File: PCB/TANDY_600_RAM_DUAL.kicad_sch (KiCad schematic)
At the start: 7 parts, among them CN1 TANDY_600_RAM_BUS, CN2 TANDY_600_RAM_BUS, U1 AS6C4008, U2 74HC148, U3 74LVC1G02

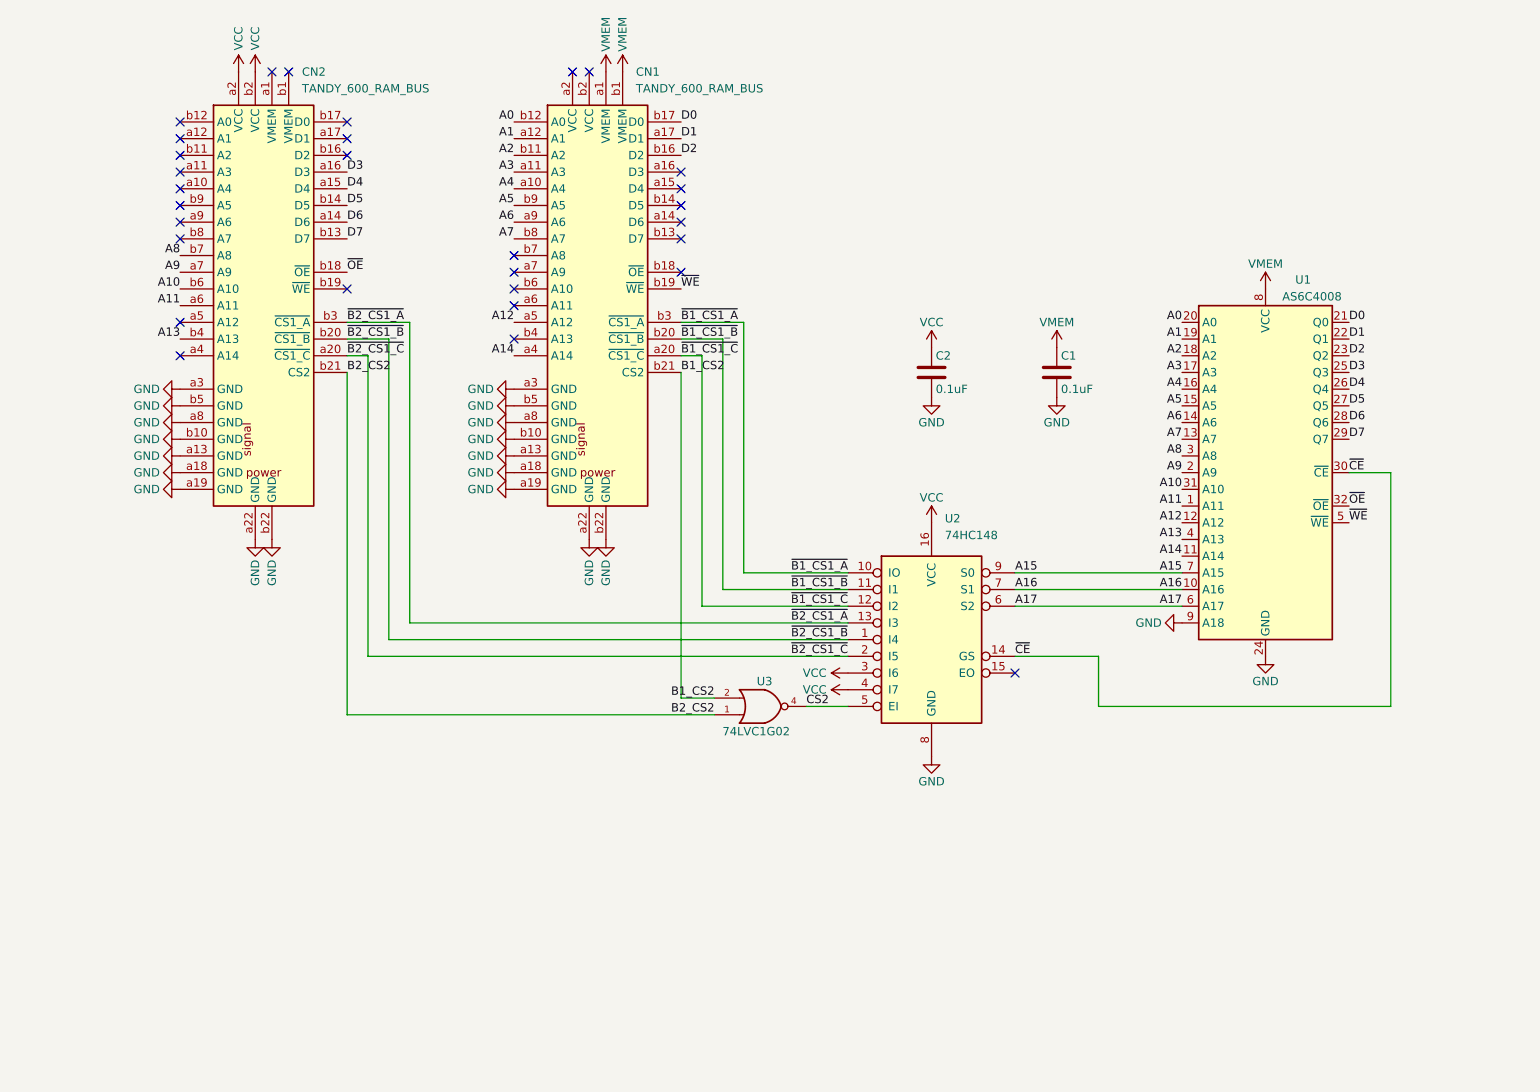
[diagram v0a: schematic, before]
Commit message: footprints, ground paths
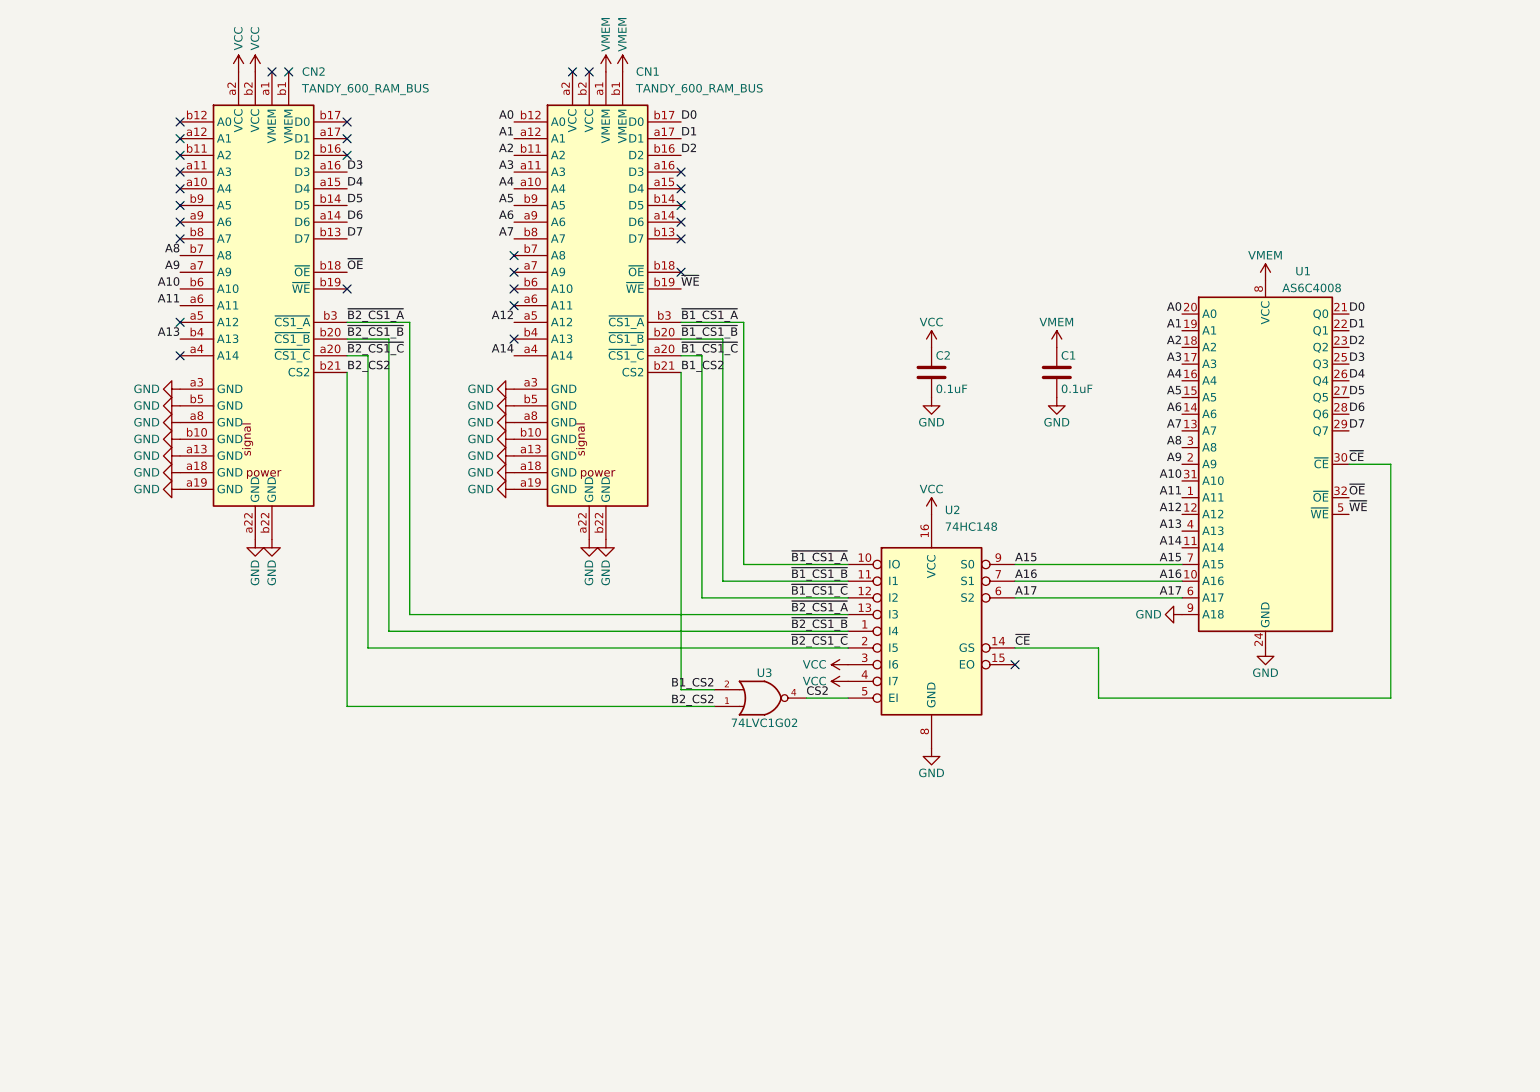
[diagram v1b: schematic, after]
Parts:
- CN1, CN2: footprint 000_LOCAL:DIN41612-2x22_male_vertical_bare_pins -> 000_LOCAL:DIN-41612_02x22_male_vertical_bare_pins
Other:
- moved on the sheet: U1, U2, U3

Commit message: support 256Kx8 chip on dual
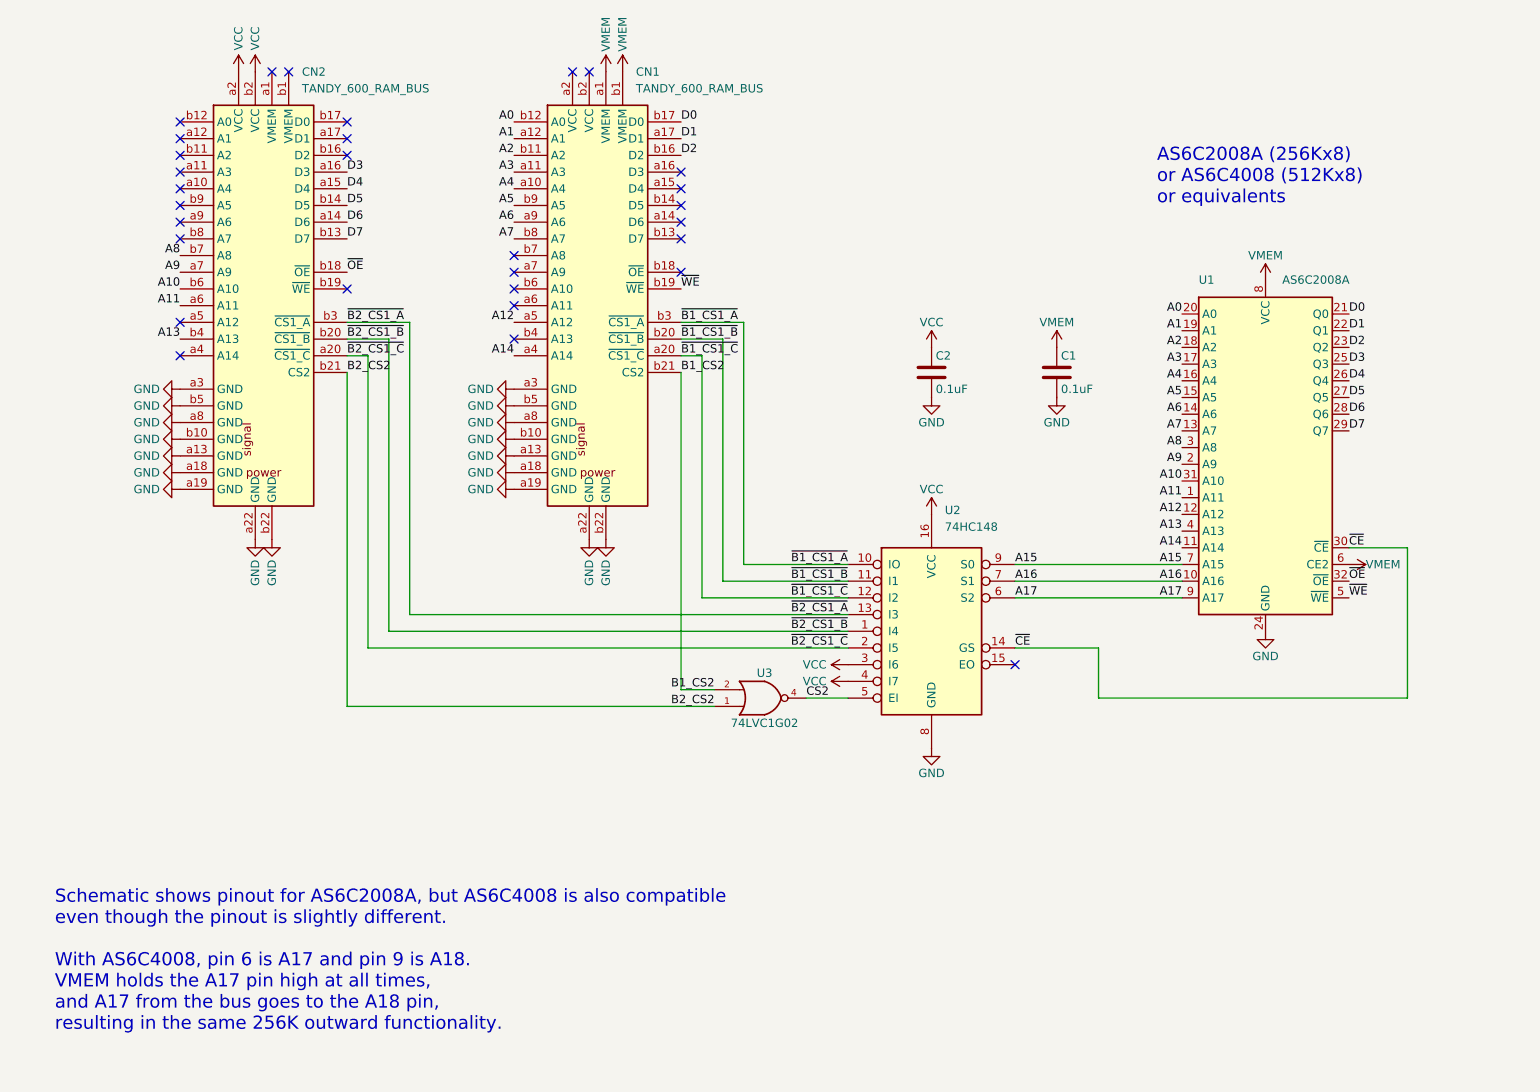
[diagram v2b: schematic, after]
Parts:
- U1: value AS6C4008 -> AS6C2008A; symbol 000_LOCAL:AS6C4008_TSOP-I_sTSOP -> 000_LOCAL:AS6C2008_TSOP-I-32
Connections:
- net A17: now also U1.9 (A17); no longer U1.6 (A17)
- net GND: no longer U1.9 (A18)
- net VMEM: now also U1.6 (CE2)
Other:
- note added: "AS6C2008A (256Kx8) or AS6C4008 (512Kx8) or equivalents"
- note added: "Schematic shows pinout for AS6C2008A, but AS6C4008 is also compatible even though the pinout is slightly different. With AS6C4008, pin 6 is A17 and pin 9 is A18. VMEM holds the A17 pin high at all times, and A17 from the bus goes to the A18 pin, resulting in the same 256K outward functionality."
- title: TANDY 600 RAM -> TANDY 600 RAM DUAL
- moved on the sheet: U1
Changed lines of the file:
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@@
   (paper "USLetter")
   (title_block
-    (title "TANDY 600 RAM")
-    (date "2022-10-20")
-    (rev "DUAL_005")
+    (title "TANDY 600 RAM DUAL")
+    (date "2022-12-22")
+    (rev "010")
     (company "Brian K. White - b.kenyon.w@gmail.com")
-    (comment 1 "LICENSE: CC-BY-SA 4.0")
+    (comment 1 "CC-BY-SA")
     (comment 2 "Originally based on Model600Sram_v1.1 by Jayeson Lee-Steer")
     (comment 3 "github.com/bkw777/TANDY_600_RAM")
@@
     (stroke (width 0) (type default) (color 0 0 0 0))
   )
-  (wire (pts (xy 228.6 104.14) (xy 228.6 139.7))
+  (wire (pts (xy 231.14 116.84) (xy 231.14 139.7))
     (stroke (width 0) (type default) (color 0 0 0 0))
   )
@@
     (stroke (width 0) (type default) (color 0 0 0 0))
   )
+  (wire (pts (xy 222.25 116.84) (xy 231.14 116.84))
+    (stroke (width 0) (type default) (color 0 0 0 0))
+  )
   (wire (pts (xy 123.825 124.46) (xy 146.05 124.46))
     (stroke (width 0) (type default) (color 0 0 0 0))
@@
     (stroke (width 0) (type default) (color 0 0 0 0))
   )
-  (wire (pts (xy 184.15 139.7) (xy 228.6 139.7))
+  (wire (pts (xy 184.15 139.7) (xy 231.14 139.7))
     (stroke (width 0) (type default) (color 0 0 0 0))
   )
@@
     (stroke (width 0) (type default) (color 0 0 0 0))
   )
-  (wire (pts (xy 228.6 104.14) (xy 222.25 104.14))
-    (stroke (width 0) (type default) (color 0 0 0 0))
-  )
   (wire (pts (xy 171.45 121.92) (xy 196.85 121.92))
     (stroke (width 0) (type default) (color 0 0 0 0))
@@
     (stroke (width 0) (type default) (color 0 0 0 0))
   )
+  (text "AS6C2008A (256Kx8)\nor AS6C4008 (512Kx8)\nor equivalents"
+    (at 193.04 64.77 0)
+    (effects (font (size 2 2)) (justify left bottom))
+  )
+  (text "Schematic shows pinout for AS6C2008A, but AS6C4008 is also compatible\neven though the pinout is slightly different.\n\nWith AS6C4008, pin 6 is A17 and pin 9 is A18.\nVMEM holds the A17 pin high at all times,\nand A17 from the bus goes to the A18 pin,\nresulting in the same 256K outward functionality.\n"
+    (at 25.4 190.5 0)
+    (effects (font (size 2 2)) (justify left bottom))
+  )
   (label "B2_CS2" (at 69.85 90.17 0)
     (effects (font (size 1.27 1.27)) (justify left bottom))
@@
     (effects (font (size 1.27 1.27)) (justify left bottom))
   )
-  (label "~{WE}" (at 222.25 111.76 0)
+  (label "~{WE}" (at 222.25 124.46 0)
     (effects (font (size 1.27 1.27)) (justify left bottom))
   )
@@
     (effects (font (size 1.27 1.27)) (justify right bottom))
   )
-  (label "~{OE}" (at 222.25 109.22 0)
+  (label "~{OE}" (at 222.25 121.92 0)
     (effects (font (size 1.27 1.27)) (justify left bottom))
   )
@@
     (effects (font (size 1.27 1.27)) (justify right bottom))
   )
-  (label "~{CE}" (at 222.25 104.14 0)
+  (label "~{CE}" (at 222.25 116.84 0)
     (effects (font (size 1.27 1.27)) (justify left bottom))
   )
@@
     (pin "1")
   )
-  (symbol (lib_id "000_LOCAL:AS6C4008_TSOP-I_sTSOP") (at 209.55 101.6 0) (unit 1)
-    (in_bom yes) (on_board yes)
-    (property "Reference" "U1" (id 0) (at 215.265 74.803 0))
-    (property "Value" "AS6C4008" (id 1) (at 212.09 78.105 0)
+  (symbol (lib_id "000_LOCAL:AS6C2008_TSOP-I-32") (at 209.55 100.33 0) (unit 1)
+    (in_bom yes) (on_board yes)
+    (property "Reference" "U1" (id 0) (at 199.39 76.835 0)
       (effects (font (size 1.27 1.27)) (justify left bottom))
     )
-    (property "Footprint" "000_LOCAL:TSOP32-dual" (id 2) (at 209.55 101.6 0)
-      (effects (font (size 1.27 1.27)) hide)
-    )
-    (property "Datasheet" "https://www.alliancememory.com/wp-content/uploads/pdf/AS6C4008.pdf" (id 3) (at 209.55 101.6 0)
+    (property "Value" "AS6C2008A" (id 1) (at 212.09 76.835 0)
+      (effects (font (size 1.27 1.27)) (justify left bottom))
+    )
+    (property "Footprint" "000_LOCAL:TSOP32-dual" (id 2) (at 209.55 100.33 0)
+      (effects (font (size 1.27 1.27)) hide)
+    )
+    (property "Datasheet" "https://www.alliancememory.com/wp-content/uploads/pdf/AS6C4008.pdf" (id 3) (at 209.55 102.87 0)
       (effects (font (size 1.27 1.27)) hide)
     )
@@
     (pin "1")
   )
-  (symbol (lib_id "000_LOCAL:GND") (at 209.55 132.08 0) (unit 1)
-    (in_bom yes) (on_board yes)
-    (property "Reference" "#PWR0121" (id 0) (at 209.55 138.43 0)
-      (effects (font (size 1.27 1.27)) hide)
-    )
-    (property "Value" "GND" (id 1) (at 209.55 135.89 0))
-    (property "Footprint" "" (id 2) (at 209.55 132.08 0)
-      (effects (font (size 1.27 1.27)) hide)
-    )
-    (property "Datasheet" "" (id 3) (at 209.55 132.08 0)
+  (symbol (lib_id "000_LOCAL:GND") (at 209.55 129.54 0) (unit 1)
+    (in_bom yes) (on_board yes)
+    (property "Reference" "#PWR0121" (id 0) (at 209.55 135.89 0)
+      (effects (font (size 1.27 1.27)) hide)
+    )
+    (property "Value" "GND" (id 1) (at 209.55 133.35 0))
+    (property "Footprint" "" (id 2) (at 209.55 129.54 0)
+      (effects (font (size 1.27 1.27)) hide)
+    )
+    (property "Datasheet" "" (id 3) (at 209.55 129.54 0)
       (effects (font (size 1.27 1.27)) hide)
     )
@@
     (pin "1")
   )
-  (symbol (lib_id "000_LOCAL:GND") (at 196.85 127 270) (unit 1)
-    (in_bom yes) (on_board yes)
-    (property "Reference" "#PWR0108" (id 0) (at 190.5 127 0)
-      (effects (font (size 1.27 1.27)) hide)
-    )
-    (property "Value" "GND" (id 1) (at 191.77 127 90))
-    (property "Footprint" "" (id 2) (at 196.85 127 0)
-      (effects (font (size 1.27 1.27)) hide)
-    )
-    (property "Datasheet" "" (id 3) (at 196.85 127 0)
+  (symbol (lib_id "000_LOCAL:VMEM") (at 222.25 119.38 270) (unit 1)
+    (in_bom yes) (on_board yes)
+    (property "Reference" "#PWR0108" (id 0) (at 218.44 119.38 0)
+      (effects (font (size 1.27 1.27)) hide)
+    )
+    (property "Value" "VMEM" (id 1) (at 224.79 119.38 90)
+      (effects (font (size 1.27 1.27)) (justify left))
+    )
+    (property "Footprint" "" (id 2) (at 222.25 119.38 0)
+      (effects (font (size 1.27 1.27)) hide)
+    )
+    (property "Datasheet" "" (id 3) (at 222.25 119.38 0)
       (effects (font (size 1.27 1.27)) hide)
     )
@@
       (reference "#PWR0107") (unit 1) (value "VCC") (footprint "")
     )
-    (path "/cc9803f3-bb05-4bf5-b035-7c2270f51b41"
-      (reference "#PWR0108") (unit 1) (value "GND") (footprint "")
+    (path "/d329f241-8a5a-4dd9-bd17-b03a5b12561c"
+      (reference "#PWR0108") (unit 1) (value "VMEM") (footprint "")
     )
     (path "/b42ca7e3-79f8-402f-ba75-ec58cce09748"
@@
     )
     (path "/00000000-0000-0000-0000-0000613c8a04"
-      (reference "U1") (unit 1) (value "AS6C4008") (footprint "000_LOCAL:TSOP32-dual")
+      (reference "U1") (unit 1) (value "AS6C2008A") (footprint "000_LOCAL:TSOP32-dual")
     )
     (path "/88b9c531-ca53-4b2a-bf55-7a2b00d5c199"
